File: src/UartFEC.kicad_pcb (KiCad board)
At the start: 2 copper layers, 24 x 27.9 mm, 15 parts, among them J1 B3B-XH-A, P1 105444-0001, U1 FT232RL

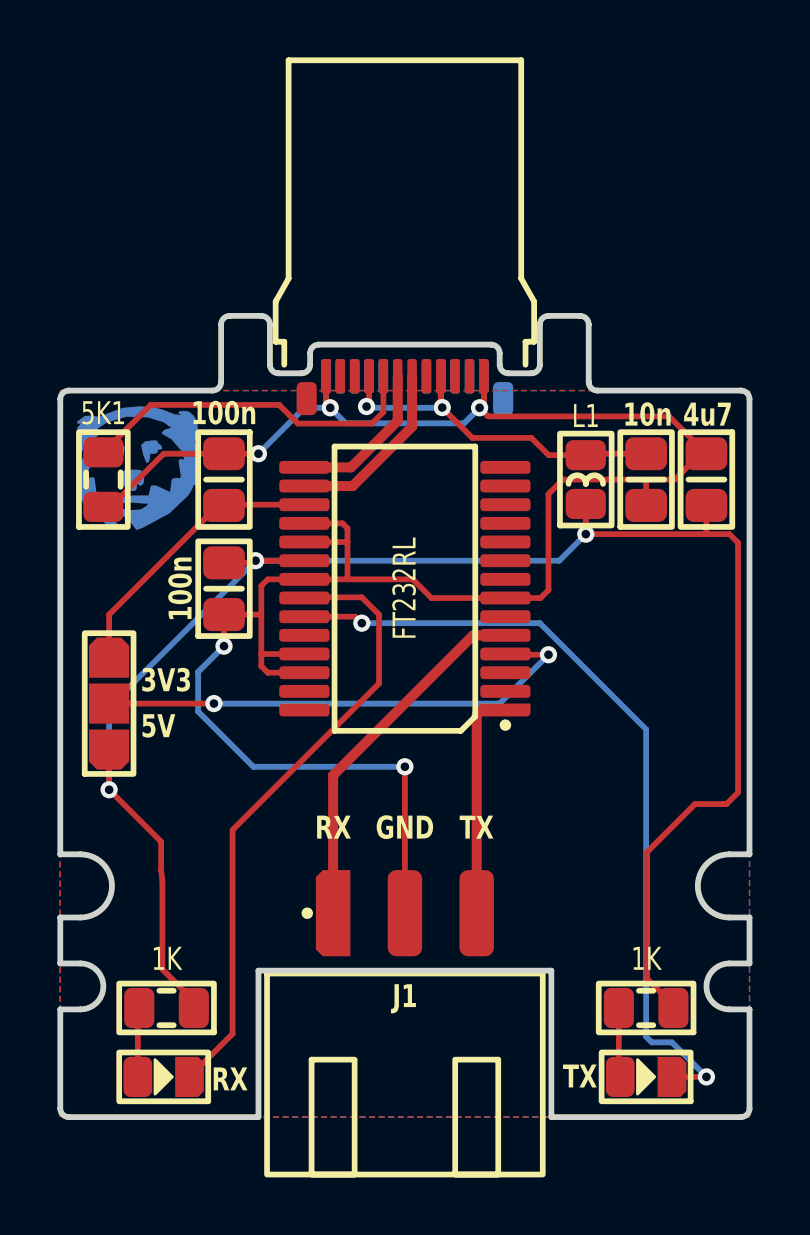
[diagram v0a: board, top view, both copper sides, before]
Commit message: Added TVS protection
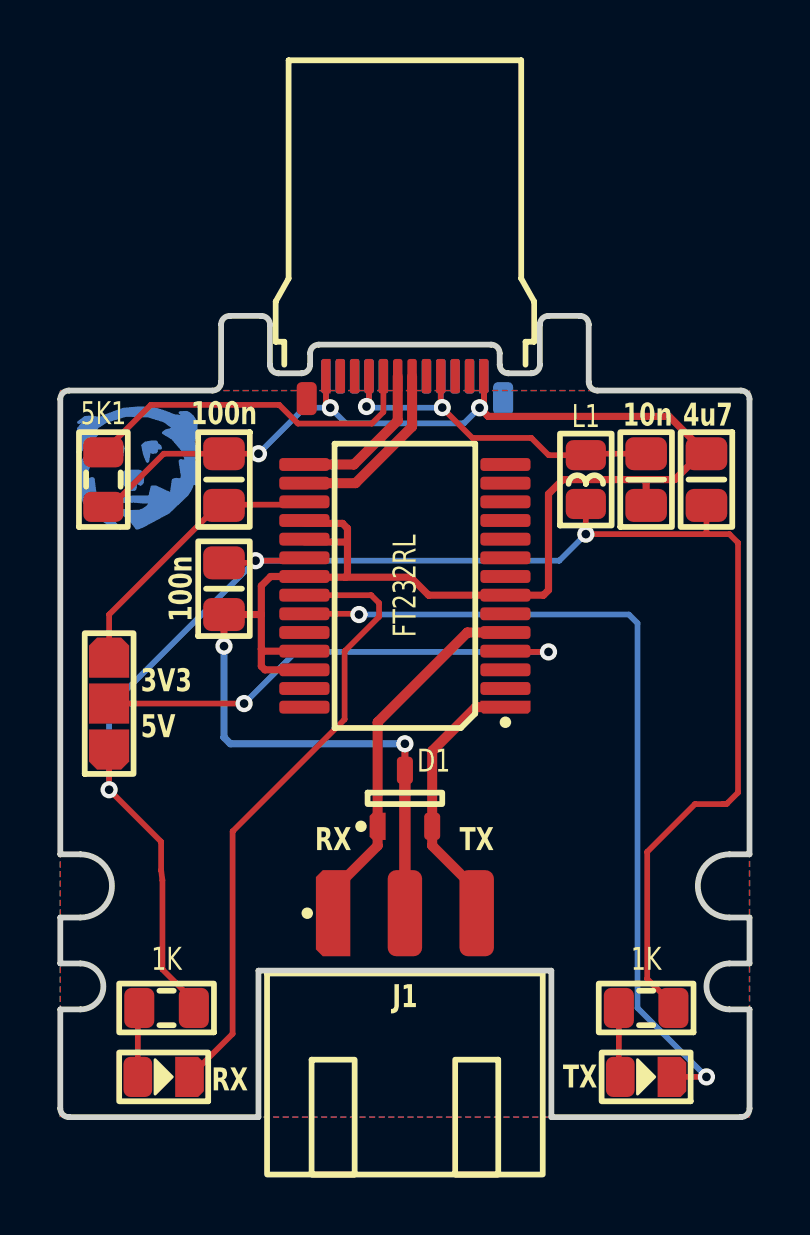
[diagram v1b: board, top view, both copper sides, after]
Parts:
- added D1: SM05T1G, Medo64:D TVS SM05T1G (SOT23-3), F.Cu at (32.0, 36.8)
- moved U1 0.10 mm to (32.0, 29.4)
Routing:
- net LED_TXD: track 28.1 -> 29.7 mm
- net TXD: track 7.97 -> 9.47 mm
- net LED_RXD: track 20.9 -> 21.9 mm
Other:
- board text removed: "GND"
